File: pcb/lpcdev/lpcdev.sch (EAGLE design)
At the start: 106 parts, among them IC1 LPC1517BJD48, IC2 DRV8313, IC3 FT231X, IC4 LP2985-3V3, IC5 DRV8313, IC6 DRV8313, Q1 16MHz

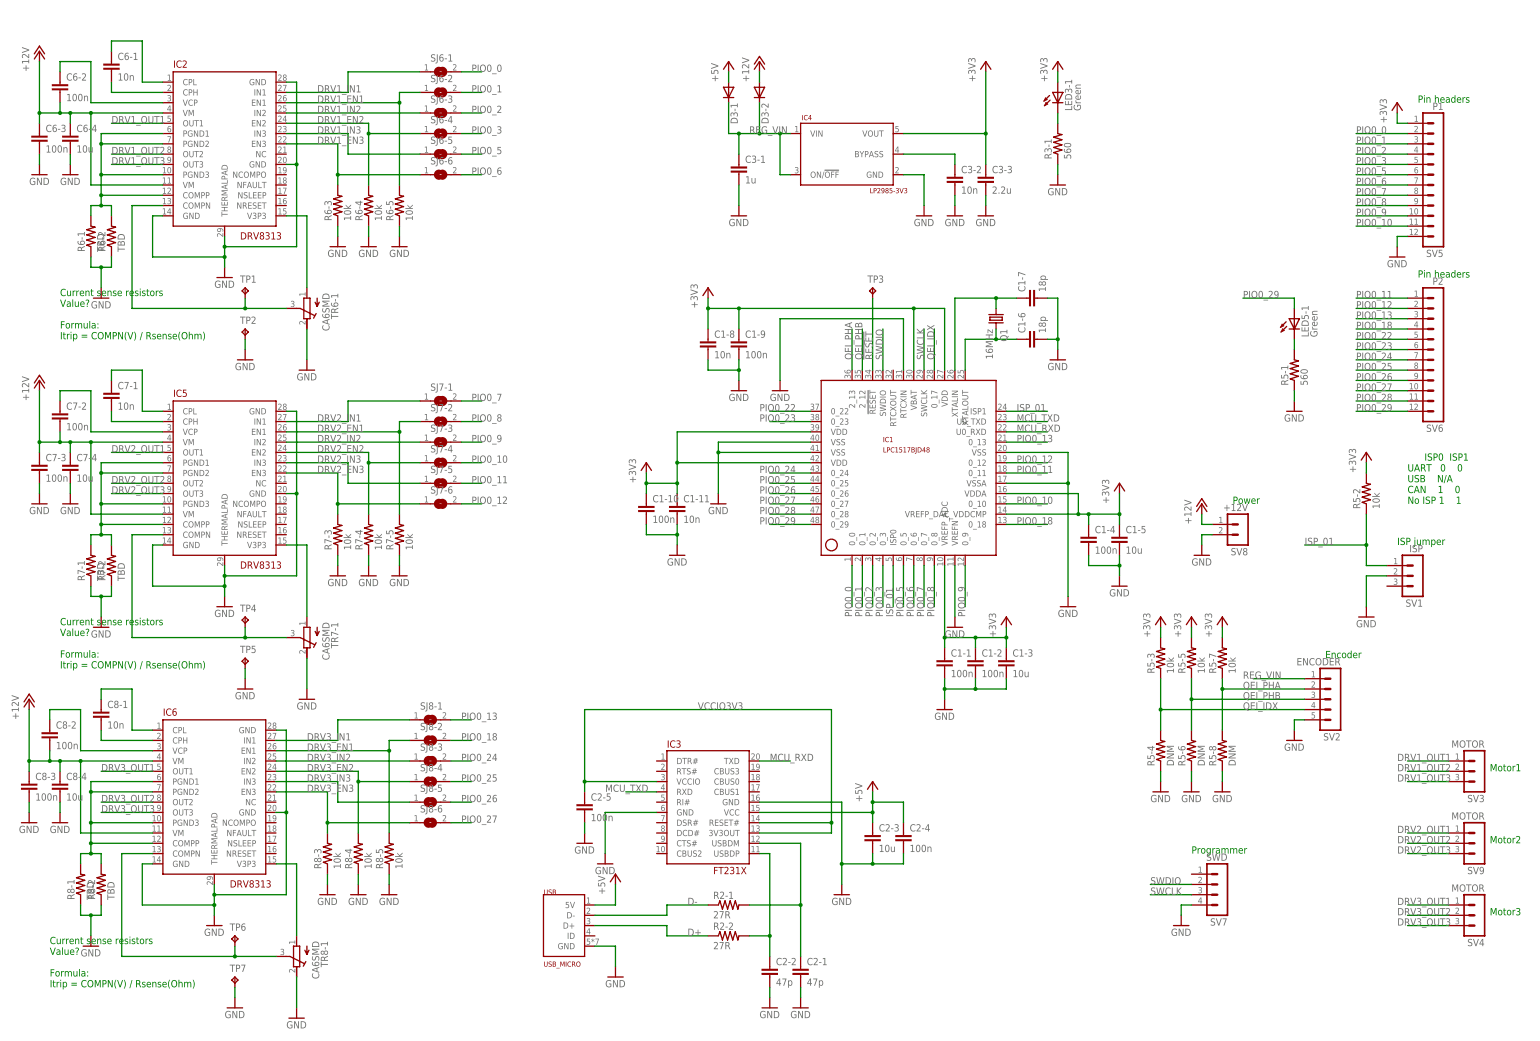
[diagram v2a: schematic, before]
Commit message: rough routing (no gnd)
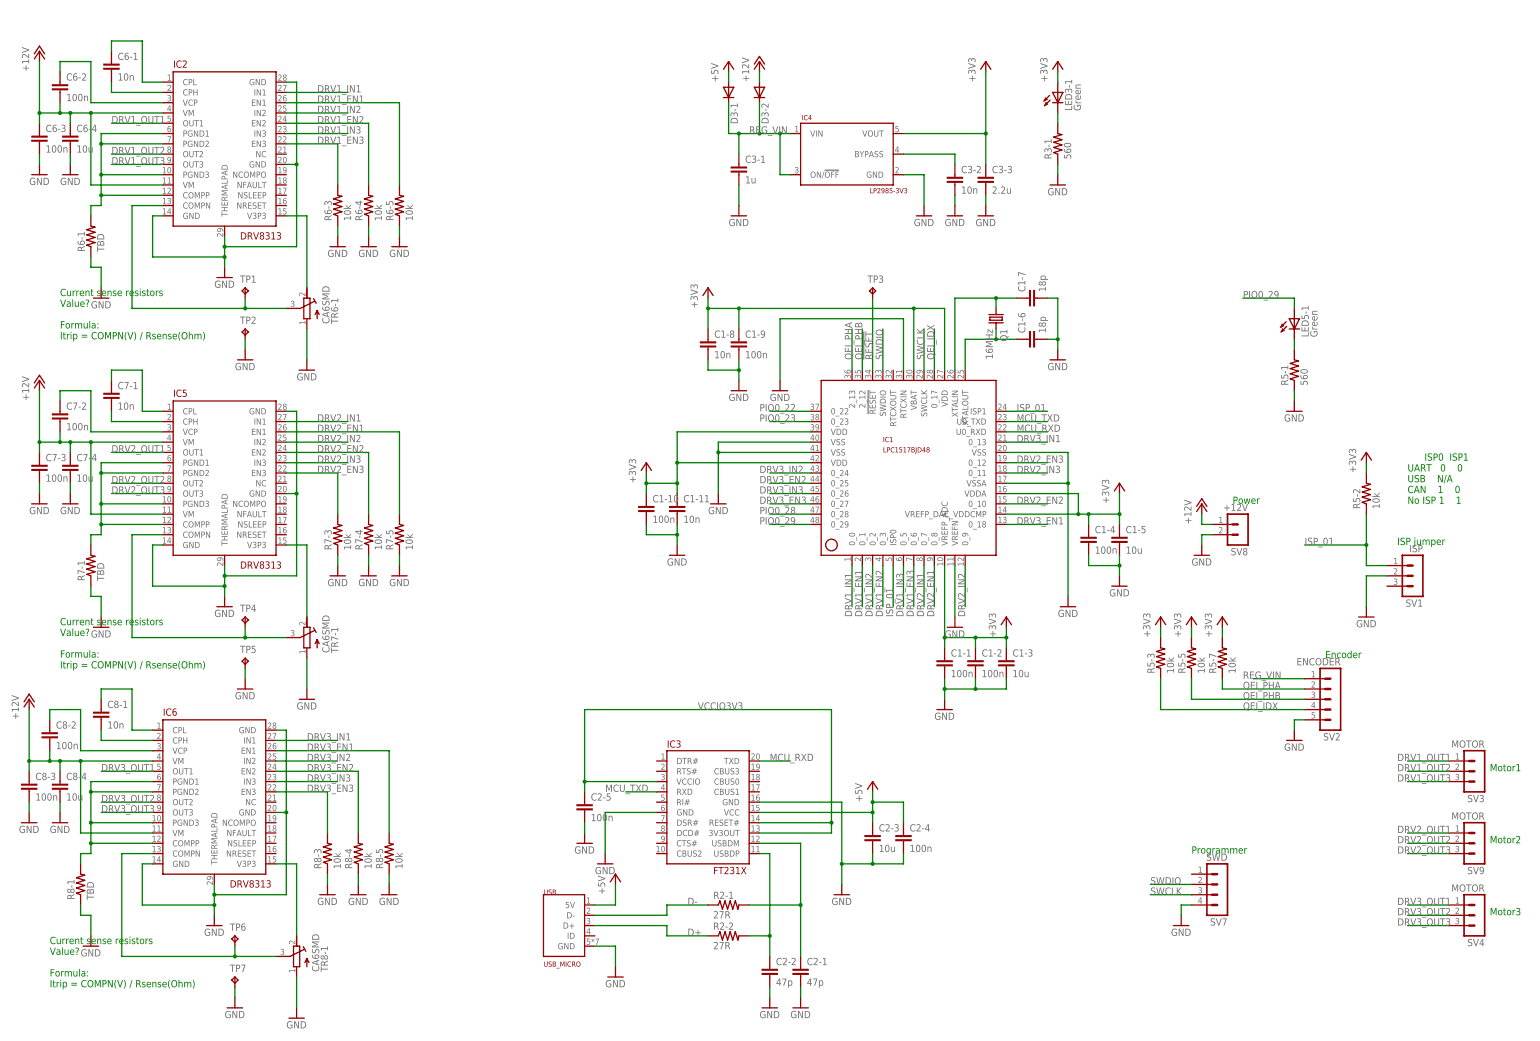
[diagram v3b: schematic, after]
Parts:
- removed R5-4, R5-6, R5-8: DNM, rcl:R-US_R0603
- removed R6-2, R7-2, R8-2: TBD, rcl:R-US_R0805
- removed SJ6-1, SJ6-2, SJ6-3, SJ6-4, SJ6-5, SJ6-6, SJ7-1, SJ7-2, SJ7-3, SJ7-4, SJ7-5, SJ7-6, SJ8-1, SJ8-2, SJ8-3, SJ8-4, SJ8-5, SJ8-6: (no value), jumper:SJ
- removed SV5: P1, con-lstb:MA12-1
- removed SV6: P2, con-lstb:MA12-1
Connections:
- removed net PIO0_0: IC1.0_0, SJ6-1.2, SV5.2
- removed net PIO0_1: IC1.0_1, SJ6-2.2, SV5.3
- removed net PIO0_10: IC1.0_10, SJ7-4.2, SV5.11
- removed net PIO0_11: IC1.0_11, SJ7-5.2, SV6.1
- removed net PIO0_12: IC1.0_12, SJ7-6.2, SV6.2
- removed net PIO0_13: IC1.0_13, SJ8-1.2, SV6.3
- removed net PIO0_18: IC1.0_18, SJ8-2.2, SV6.4
- removed net PIO0_2: IC1.0_2, SJ6-3.2, SV5.4
- removed net PIO0_24: IC1.0_24, SJ8-3.2, SV6.7
- removed net PIO0_25: IC1.0_25, SJ8-4.2, SV6.8
- removed net PIO0_26: IC1.0_26, SJ8-5.2, SV6.9
- removed net PIO0_27: IC1.0_27, SJ8-6.2, SV6.10
- removed net PIO0_3: IC1.0_3, SJ6-4.2, SV5.5
- removed net PIO0_5: IC1.0_5, SJ6-5.2, SV5.6
- removed net PIO0_6: IC1.0_6, SJ6-6.2, SV5.7
- removed net PIO0_7: IC1.0_7, SJ7-1.2, SV5.8
- removed net PIO0_8: IC1.0_8, SJ7-2.2, SV5.9
- removed net PIO0_9: IC1.0_9, SJ7-3.2, SV5.10
- net +3V3: no longer SV5.1
- net DRV1_3V3: now also TR6-1.E; no longer TR6-1.A
- net DRV1_COMPP: no longer R6-2.2
- net DRV1_EN1: now also IC1.0_1; no longer SJ6-2.1
- net DRV1_EN2: now also IC1.0_3; no longer SJ6-4.1
- net DRV1_EN3: now also IC1.0_6; no longer SJ6-6.1
- net DRV1_IN1: now also IC1.0_0; no longer SJ6-1.1
- net DRV1_IN2: now also IC1.0_2; no longer SJ6-3.1
- net DRV1_IN3: now also IC1.0_5; no longer SJ6-5.1
- net DRV2_3V1: now also TR7-1.E; no longer TR7-1.A
- net DRV2_COMPP1: no longer R7-2.2
- net DRV2_EN1: now also IC1.0_8; no longer SJ7-2.1
- net DRV2_EN2: now also IC1.0_10; no longer SJ7-4.1
- net DRV2_EN3: now also IC1.0_12; no longer SJ7-6.1
- net DRV2_IN1: now also IC1.0_7; no longer SJ7-1.1
- net DRV2_IN2: now also IC1.0_9; no longer SJ7-3.1
- net DRV2_IN3: now also IC1.0_11; no longer SJ7-5.1
- net DRV3_3V2: now also TR8-1.E; no longer TR8-1.A
- net DRV3_COMPP2: no longer R8-2.2
- net DRV3_EN1: now also IC1.0_18; no longer SJ8-2.1
- net DRV3_EN2: now also IC1.0_25; no longer SJ8-4.1
- net DRV3_EN3: now also IC1.0_27; no longer SJ8-6.1
- net DRV3_IN1: now also IC1.0_13; no longer SJ8-1.1
- net DRV3_IN2: now also IC1.0_24; no longer SJ8-3.1
- net DRV3_IN3: now also IC1.0_26; no longer SJ8-5.1
- net GND: now also TR6-1.A, TR7-1.A, TR8-1.A; no longer R5-4.1, R5-6.1, R5-8.1, R6-2.1, R7-2.1, R8-2.1, SV5.12, TR6-1.E, TR7-1.E, TR8-1.E
- net PIO0_22: no longer SV6.5
- net PIO0_23: no longer SV6.6
- net PIO0_28: no longer SV6.11
- net PIO0_29: no longer SV6.12
- net QEI_IDX: no longer R5-4.2
- net QEI_PHA: no longer R5-8.2
- net QEI_PHB: no longer R5-6.2
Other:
- note removed: "Pin headers"
- moved on the sheet: TR6-1, TR7-1, TR8-1

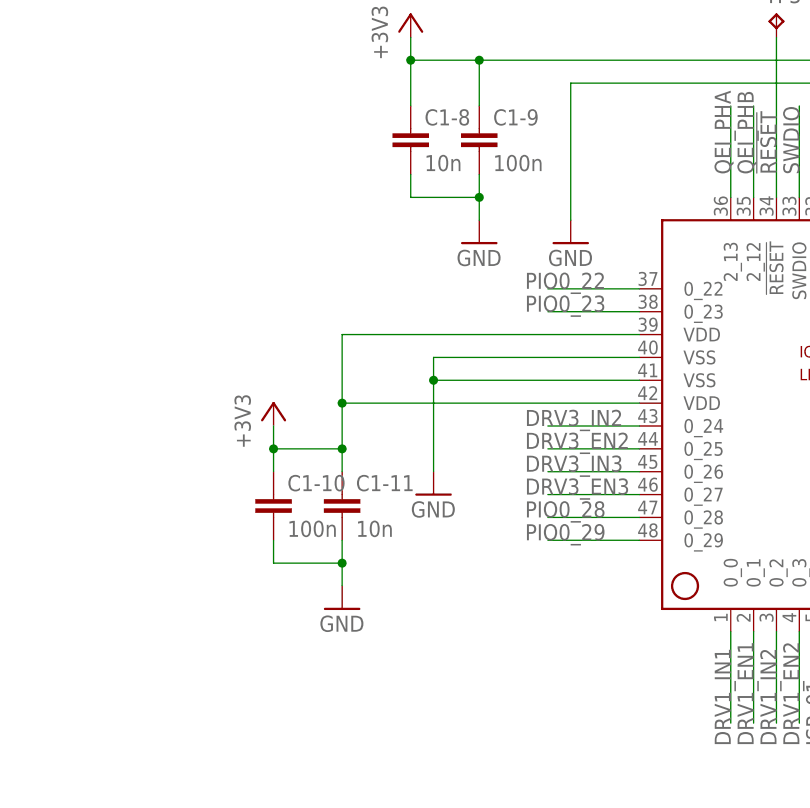
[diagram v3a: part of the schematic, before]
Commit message: Routing complete, ERC and DRC is OK
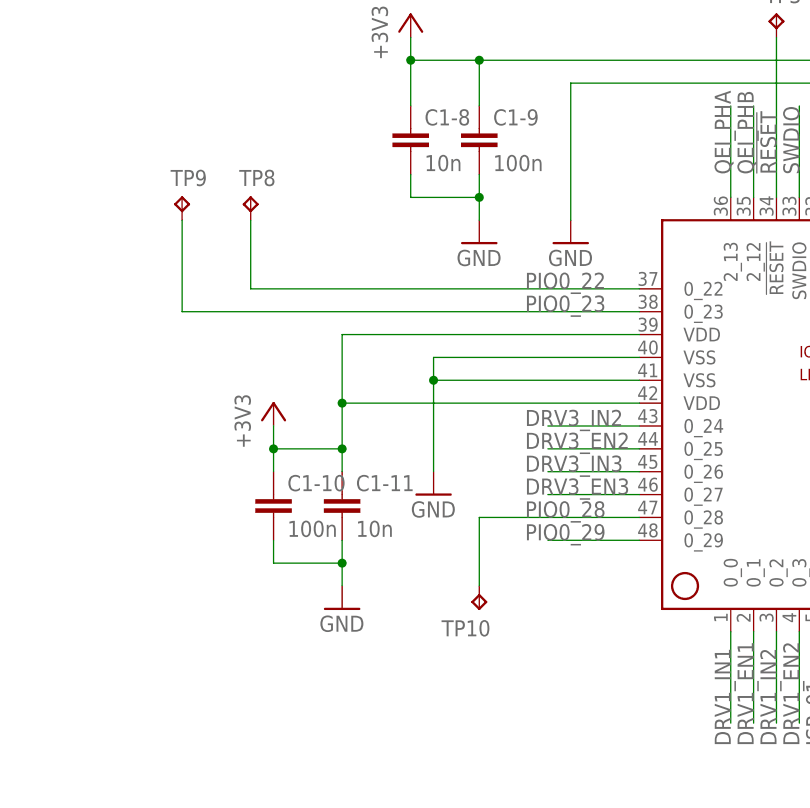
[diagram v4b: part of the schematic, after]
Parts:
- added TP10, TP8, TP9: TPB1,27, testpad:TPB1,27
- SV1, SV3, SV4, SV9: device con-lstb:MA03-1 -> lpclib:MA03-1
- SV2: device con-lstb:MA05-1 -> lpclib:MA05-1
- SV7: device con-lstb:MA04-1 -> lpclib:MA04-1
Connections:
- net PIO0_22: now also TP8.TP
- net PIO0_23: now also TP9.TP
- net PIO0_28: now also TP10.TP
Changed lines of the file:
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@@
 <?xml version="1.0" encoding="utf-8"?>
 <!DOCTYPE eagle SYSTEM "eagle.dtd">
-<eagle version="7.5.0">
+<eagle version="7.3.0">
 <drawing>
 <settings>
@@
 <part name="R3-1" library="rcl" deviceset="R-US_" device="R0603" value="560"/>
 <part name="GND17" library="supply" deviceset="GND" device=""/>
-<part name="SV1" library="con-lstb" deviceset="MA03-1" device="" value="ISP"/>
-<part name="SV2" library="con-lstb" deviceset="MA05-1" device="" value="ENCODER"/>
-<part name="SV4" library="con-lstb" deviceset="MA03-1" device="" value="MOTOR"/>
+<part name="SV1" library="lpclib" deviceset="MA03-1" device="" value="ISP"/>
+<part name="SV2" library="lpclib" deviceset="MA05-1" device="" value="ENCODER"/>
+<part name="SV4" library="lpclib" deviceset="MA03-1" device="" value="MOTOR"/>
 <part name="C2-4" library="rcl" deviceset="C-EU" device="C0603" value="100n"/>
 <part name="R5-7" library="rcl" deviceset="R-US_" device="R0603" value="10k"/>
@@
 <part name="GND33" library="supply" deviceset="GND" device=""/>
 <part name="TP3" library="testpad" deviceset="TP" device="B1,27"/>
-<part name="SV7" library="con-lstb" deviceset="MA04-1" device="" value="SWD"/>
+<part name="SV7" library="lpclib" deviceset="MA04-1" device="" value="SWD"/>
 <part name="GND34" library="supply" deviceset="GND" device=""/>
 <part name="R6-5" library="rcl" deviceset="R-US_" device="R0603" value="10k"/>
@@
 <part name="C8-4" library="rcl" deviceset="C-EU" device="C0805" value="10u"/>
 <part name="GND56" library="supply" deviceset="GND" device=""/>
-<part name="SV3" library="con-lstb" deviceset="MA03-1" device="" value="MOTOR"/>
-<part name="SV9" library="con-lstb" deviceset="MA03-1" device="" value="MOTOR"/>
+<part name="SV3" library="lpclib" deviceset="MA03-1" device="" value="MOTOR"/>
+<part name="SV9" library="lpclib" deviceset="MA03-1" device="" value="MOTOR"/>
+<part name="TP8" library="testpad" deviceset="TP" device="B1,27"/>
+<part name="TP9" library="testpad" deviceset="TP" device="B1,27"/>
+<part name="TP10" library="testpad" deviceset="TP" device="B1,27"/>
 </parts>
 <sheets>
@@
 <instance part="SV3" gate="G$1" x="309.88" y="-73.66" rot="R180"/>
 <instance part="SV9" gate="G$1" x="309.88" y="-91.44" rot="R180"/>
+<instance part="TP8" gate="G$1" x="101.6" y="25.4"/>
+<instance part="TP9" gate="G$1" x="93.98" y="25.4"/>
+<instance part="TP10" gate="G$1" x="127" y="-20.32" rot="R180"/>
 </instances>
 <busses>
@@
 <net name="PIO0_22" class="0">
 <segment>
-<wire x1="144.78" y1="15.24" x2="134.62" y2="15.24" width="0.1524" layer="91"/>
 <label x="132.08" y="15.24" size="1.778" layer="95"/>
 <pinref part="IC1" gate="G$1" pin="0_22"/>
+<pinref part="TP8" gate="G$1" pin="TP"/>
+<wire x1="144.78" y1="15.24" x2="101.6" y2="15.24" width="0.1524" layer="91"/>
+<wire x1="101.6" y1="15.24" x2="101.6" y2="22.86" width="0.1524" layer="91"/>
 </segment>
 </net>
 <net name="PIO0_23" class="0">
 <segment>
-<wire x1="144.78" y1="12.7" x2="134.62" y2="12.7" width="0.1524" layer="91"/>
 <label x="132.08" y="12.7" size="1.778" layer="95"/>
 <pinref part="IC1" gate="G$1" pin="0_23"/>
+<pinref part="TP9" gate="G$1" pin="TP"/>
+<wire x1="144.78" y1="12.7" x2="93.98" y2="12.7" width="0.1524" layer="91"/>
+<wire x1="93.98" y1="12.7" x2="93.98" y2="22.86" width="0.1524" layer="91"/>
 </segment>
 </net>
 <net name="PIO0_28" class="0">
 <segment>
-<wire x1="144.78" y1="-10.16" x2="134.62" y2="-10.16" width="0.1524" layer="91"/>
+<wire x1="144.78" y1="-10.16" x2="127" y2="-10.16" width="0.1524" layer="91"/>
 <label x="132.08" y="-10.16" size="1.778" layer="95"/>
 <pinref part="IC1" gate="G$1" pin="0_28"/>
+<wire x1="127" y1="-10.16" x2="127" y2="-17.78" width="0.1524" layer="91"/>
+<pinref part="TP10" gate="G$1" pin="TP"/>
 </segment>
 </net>

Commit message: final touchup and gerber generating
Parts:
- removed TP10, TP8, TP9: TPB1,27, testpad:TPB1,27
- added GPIO: GPIO, lpclib:MA03-1
- renumbered LED5-1 to L029, SV1 to ISP, SV2 to ENC, SV3 to M1, SV4 to M3, SV7 to SWD, SV8 to +12V, SV9 to M2, TP1 to ILIM1, TP3 to !R, TP4 to ILIM2, TP6 to ILIM3
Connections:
- net PIO0_22: now also GPIO.1; no longer TP8.TP
- net PIO0_23: now also GPIO.2; no longer TP9.TP
- net PIO0_28: now also GPIO.3; no longer TP10.TP
